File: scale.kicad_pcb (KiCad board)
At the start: 4 copper layers, 80 x 60 mm, 53 parts, among them J1 Conn_01x02_Pin, J2 Conn_01x04_Pin, J3 Conn_01x05_Pin, J4 Conn_01x05_Pin, Q1 S8050, Q2 S8050, Q3 MMBT3904, SW1 SW_Push, U1 HLK-10M12, U2 LM2576HVS-5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

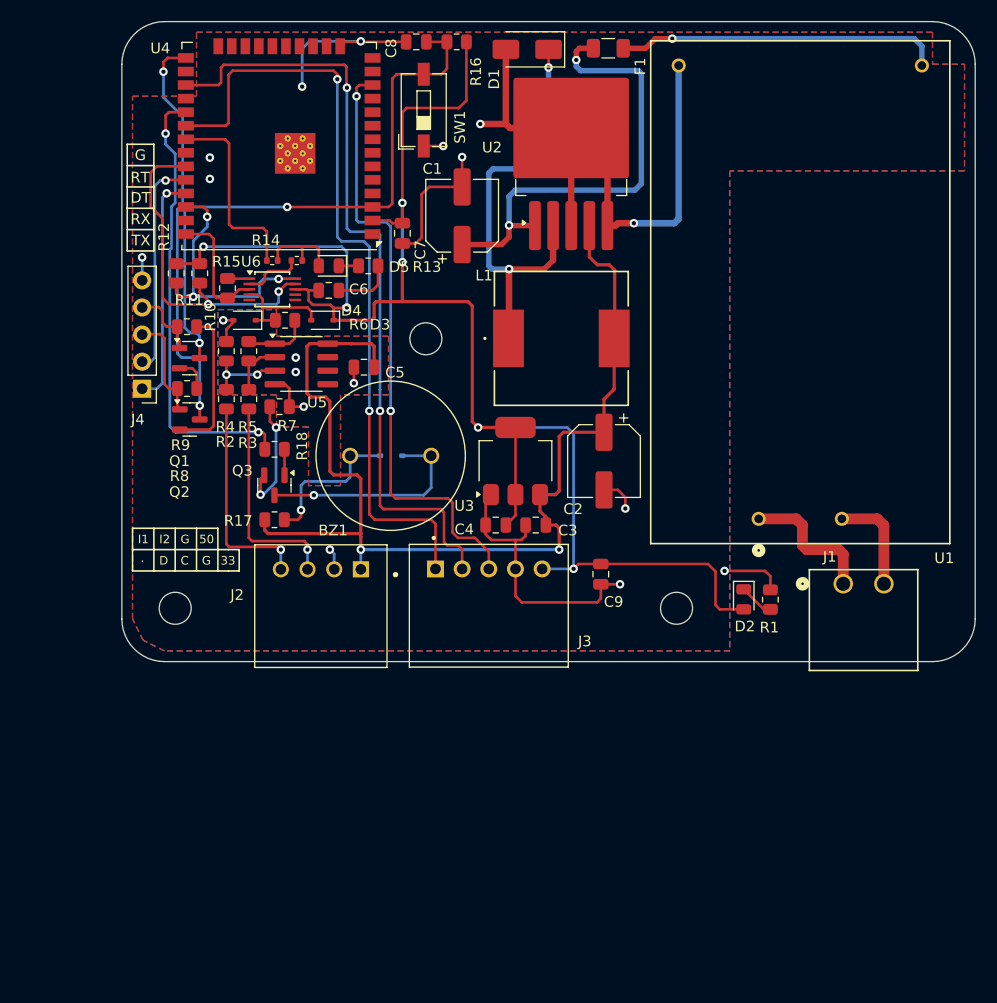
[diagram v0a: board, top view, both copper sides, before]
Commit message: change dimension
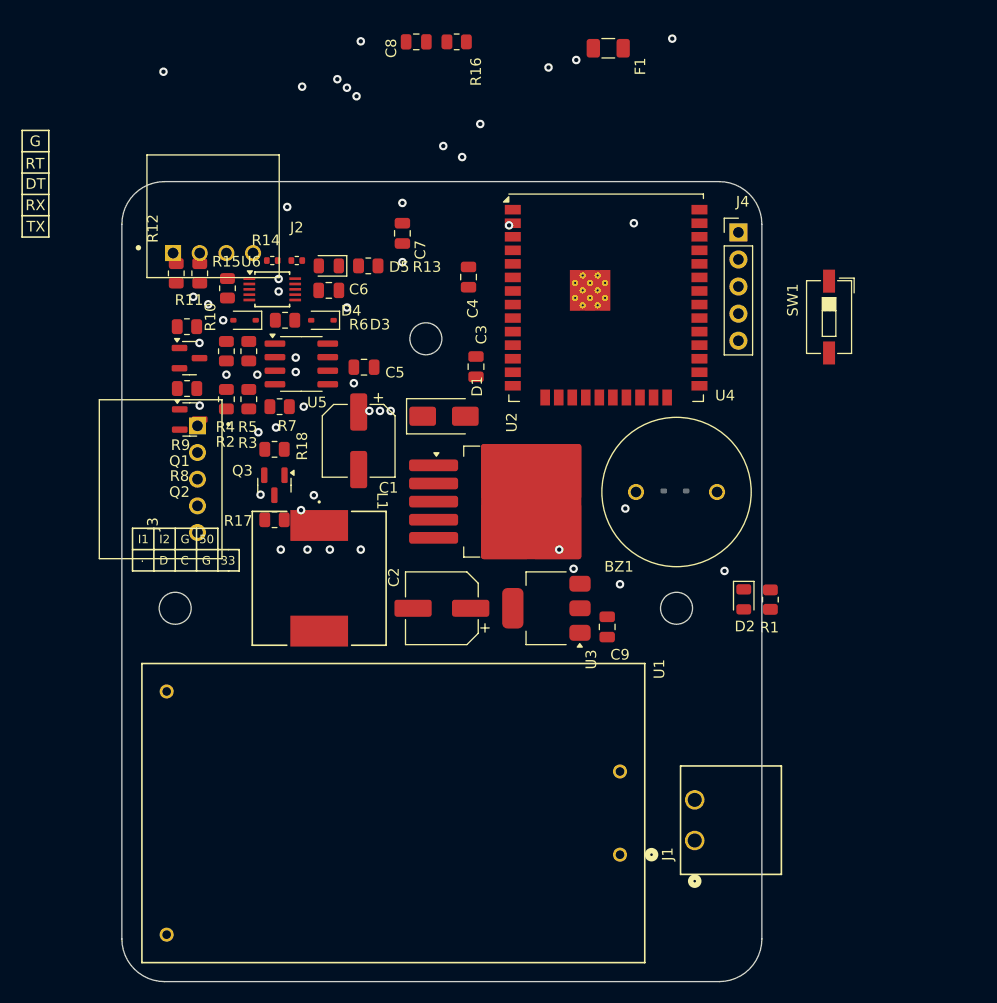
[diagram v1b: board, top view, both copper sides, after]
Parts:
- moved J4 57.8 mm to (57.8, 19.8), turned to 0 degrees
- moved SW1 42.7 mm to (66.3, 27.7), turned to -90 degrees
- moved D1 35.3 mm to (30.2, 37.0), turned to 0 degrees
- moved U1 34.1 mm to (46.7, 78.1), turned to 180 degrees
- moved U2 33.9 mm to (36.9, 45.0), turned to 0 degrees
- moved U4 33.8 mm to (45.4, 25.9), turned to 0 degrees
- moved L1 32.0 mm to (18.5, 52.2), turned to -90 degrees
- moved J2 31.3 mm to (8.55, 21.7), turned to 0 degrees
- moved J3 28.6 mm to (7.09, 42.9), turned to -90 degrees
- moved J1 27.8 mm to (53.7, 76.8), turned to 90 degrees
- moved BZ1 27.0 mm to (52.0, 44.1)
- moved D6 26.8 mm to (51.9, 44.0)
- moved C4 23.4 mm to (32.5, 23.9), turned to -90 degrees
- moved C1 23.2 mm to (22.2, 39.3), turned to -90 degrees
- moved C2 20.5 mm to (30.0, 55.0), turned to 180 degrees
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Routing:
- net GND: track 162.3 -> 0.00 mm, vias 14 -> 11
- net +3V3: track 150.1 -> 0.00 mm, vias 6 -> 4
- net +5V: track 101.2 -> 0.00 mm
- net /display/DATA: track 73.5 -> 0.00 mm, vias 2 -> 1
- net /display/DOT: track 73.5 -> 0.00 mm, vias 2 -> 1
- net /display/CLOCK: track 57.1 -> 0.00 mm, vias 2 -> 1
- net /mcu/EN: track 56.2 -> 0.00 mm
- net Net-(U2-VIN): track 43.6 -> 0.00 mm, vias 2 -> 5
- net /BUZZ: track 42.3 -> 0.00 mm, vias 2 -> 1
- net Net-(D1-K): track 41.1 -> 0.00 mm
- net /mcu/IO0: track 38.4 -> 0.00 mm
- net /mcu/SDA: track 32.2 -> 0.00 mm
- net Net-(U1-+VO): track 30.5 -> 0.00 mm
- net /mcu/SCL: track 24.5 -> 0.00 mm, vias 3 -> 2
- net /TXD: track 21.9 -> 0.00 mm, vias 1 -> 0
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- removed copper zone on B.Cu, net GND
- removed copper zone on F.Cu, net GND
- removed copper zone on In1.Cu, net GND
- removed copper zone on In2.Cu, net GND
- removed copper zone on B.Cu, net GNDA
- removed copper zone on F.Cu, net GNDA
- removed copper zone on In1.Cu, net GNDA
- removed copper zone on In2.Cu, net GNDA
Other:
- board size 80 x 60 mm -> 60 x 75 mm

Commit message: done changes
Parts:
- added J5: Conn_01x03_Pin, BBG:CONN_S3B-XH-ALFSN_JST, F.Cu at (52.0, 66.9)
- C9: moved to B.Cu
- D3, D4: value BAT60A -> SS14; footprint Diode_SMD:D_SOD-323 -> Diode_SMD:D_SMA
- moved R18 46.7 mm to (58.6, 54.9), turned to 90 degrees
- moved Q3 46.0 mm to (57.7, 58.6), turned to 180 degrees
- moved R17 44.6 mm to (58.6, 51.2), turned to 90 degrees
- moved C9 41.8 mm to (4.70, 47.9), turned to 90 degrees
- moved J4 40.1 mm to (17.8, 22.5)
- moved F1 36.1 mm to (37.0, 37.6)
- moved SW1 36.0 mm to (30.5, 23.9), turned to 0 degrees
- moved C4 34.6 mm to (45.8, 55.9)
- moved R16 30.9 mm to (33.9, 32.7), turned to -90 degrees
- moved C8 27.6 mm to (33.9, 28.8), turned to -90 degrees
- moved C3 24.2 mm to (46.5, 52.6), turned to 0 degrees
- moved R8 19.2 mm to (22.6, 24.6)
- moved Q2 18.6 mm to (22.1, 27.4)
- moved R9 17.4 mm to (22.6, 33.9)
- moved R11 17.2 mm to (24.4, 21.7)
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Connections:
- U4 pad 13: unconnected-(U4-IO14-Pad13) -> /BUT0
- U4 pad 23: unconnected-(U4-IO15-Pad23) -> /BUT1
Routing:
- net Net-(U5A-+): vias 2 -> 0
- net Net-(U2-VIN): vias 5 -> 0
- net Net-(U1-+VO): vias 1 -> 0
- net Net-(D1-K): vias 2 -> 0
- net Net-(BZ1--): vias 1 -> 0
- net GNDA: vias 5 -> 0
- net GND: vias 11 -> 3
- net /weighing_unit/IN2: vias 1 -> 0
- net /weighing_unit/IN1: vias 1 -> 0
- net /mcu/SDA: vias 2 -> 0
- net /mcu/SCL: vias 2 -> 0
- net /mcu/IO0: vias 2 -> 0
- net /mcu/EN: vias 2 -> 0
- net /display/DOT: vias 1 -> 0
- net /display/DATA: vias 1 -> 0
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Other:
- board text removed: "."
- board text removed: "33"
- board text removed: "50"
- board text removed: "C"
- board text removed: "D"
- board text removed: "I1"
- board text removed: "I2"

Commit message: start routing
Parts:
- removed J5: Conn_01x03_Pin, BBG:CONN_S3B-XH-ALFSN_JST
- removed R14, R15: 0, Resistor_SMD:R_0402_1005Metric
- added J6: Conn_01x03_Pin, BBG:CONN_S3B-XH-ALFSN_JST, F.Cu at (52.1, 66.3)
- D6: value BAT60A -> SS14; footprint Diode_SMD:D_SOD-323 -> Diode_SMD:D_SMA
- moved R4 4.43 mm to (13.0, 38.4), turned to 0 degrees
- moved D6 3.30 mm to (52.0, 40.7)
- moved U4 1.58 mm to (47.0, 25.6)
- moved R17 1.37 mm to (57.3, 51.0)
- moved SW1 1.34 mm to (31.8, 23.9)
- moved C8 1.32 mm to (34.1, 30.1), turned to 90 degrees
- moved J2 1.25 mm to (8.75, 22.9)
- moved R7 0.85 mm to (13.0, 40.6), turned to 180 degrees
- moved C5 0.80 mm to (8.90, 27.7)
- moved R16 0.72 mm to (33.4, 33.2), turned to 0 degrees
- moved C9 0.72 mm to (5.40, 47.7)
- moved Q3 0.71 mm to (57.0, 58.5)
- moved R12 0.35 mm to (21.9, 21.7)
- moved J4 0.28 mm to (17.8, 22.2)
- moved U5 0.23 mm to (11.6, 33.0)
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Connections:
- D5 pad 2: Net-(D5-A) -> /weighing_unit/RDY
- R13 pad 1: Net-(D5-K) -> GND
- R13 pad 2: GND -> Net-(D5-K)
- U4 pad 13: /BUT0 -> /BUT1
- U4 pad 16: unconnected-(U4-IO13-Pad16) -> /BUT0
- U4 pad 23: /BUT1 -> unconnected-(U4-IO15-Pad23)
- U4 pad 31: /RDY_MCU -> unconnected-(U4-IO19-Pad31)
- U6 pad 2: /RDY_ADC -> /weighing_unit/RDY
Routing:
- net +5V: track 0.00 -> 33.9 mm
- net /BUZZ: track 0.00 -> 27.9 mm
- net Net-(BZ1-+): track 0.00 -> 21.1 mm, vias 0 -> 1
- net Net-(BZ1--): track 0.00 -> 20.1 mm, vias 0 -> 1
- net GND: track 0.00 -> 12.6 mm, vias 3 -> 2
- net +3V3: track 0.00 -> 12.2 mm
- net Net-(Q3-B): track 0.00 -> 5.04 mm
- net Net-(D2-K): track 0.00 -> 2.15 mm
